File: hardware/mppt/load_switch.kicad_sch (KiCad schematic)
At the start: 13 parts, among them Q901 Q_NMOS_SGD, Q902 Q_NMOS_SGD, U901 TPSI3050

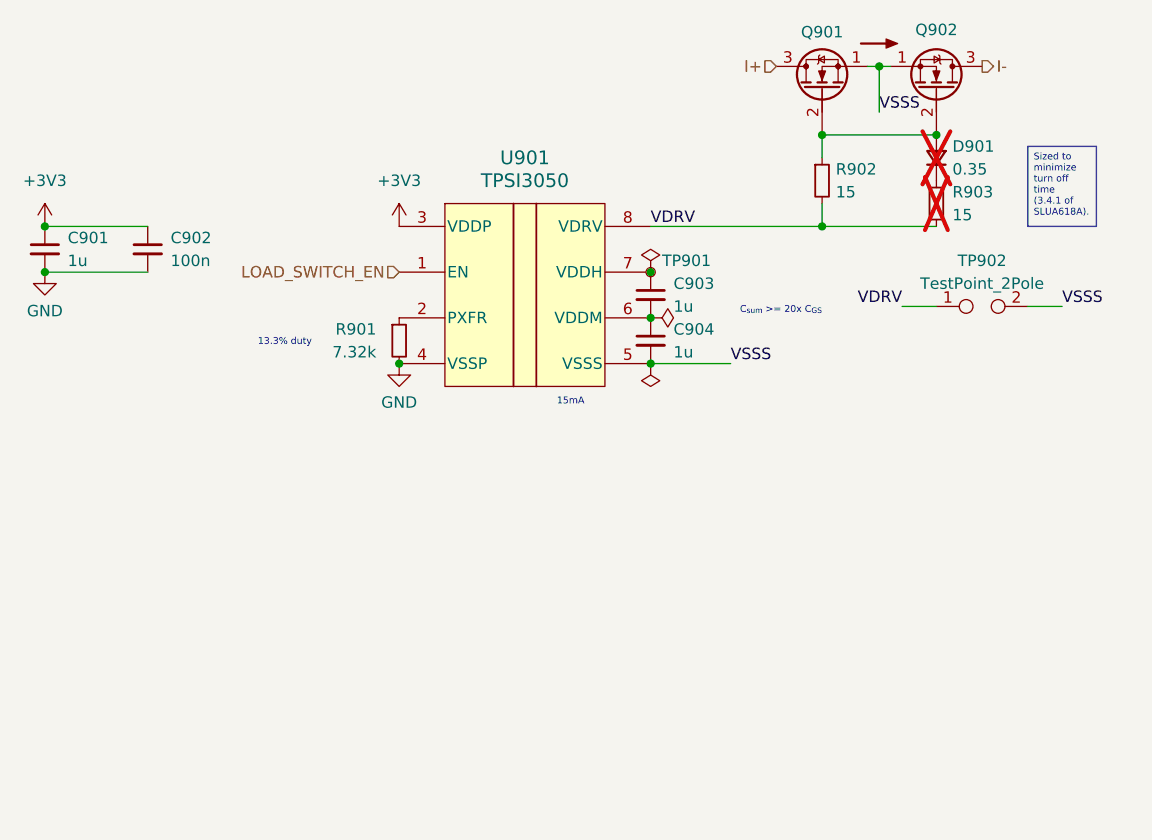
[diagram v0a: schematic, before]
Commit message: run through mppt sch, going through bom
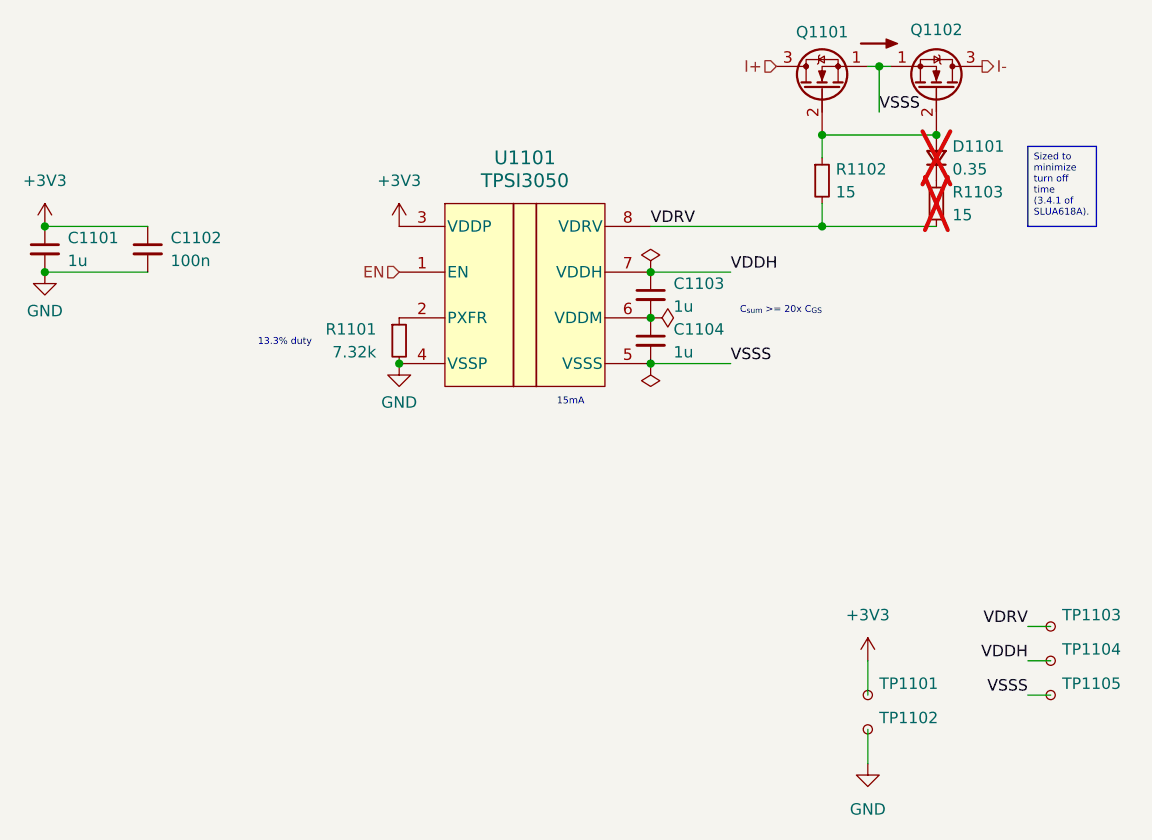
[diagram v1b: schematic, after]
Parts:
- removed TP901: TestPoint_Small, TestPoint:TestPoint_Keystone_5000-5004_Miniature, symbol Connector:TestPoint_Small
- removed TP902: TestPoint_2Pole, symbol Connector:TestPoint_2Pole
- added TP1101, TP1102: TestPoint_Small, TestPoint:TestPoint_Pad_D1.0mm, symbol Connector:TestPoint_Small
- added TP1103, TP1104, TP1105: TestPoint_Small, symbol Connector:TestPoint_Small
- C1101: renamed from C901; footprint Capacitor_SMD:C_0805_2012Metric_Pad1.18x1.45mm_HandSolder -> (none); Manufacturer Samsung Microelectronics -> Samsung Electro-Mechanics; Notes 3.3V -> 3.3V Rating
- C1102: renamed from C902; footprint Capacitor_SMD:C_0805_2012Metric_Pad1.18x1.45mm_HandSolder -> (none); Manufacturer Samsung Microelectronics -> Samsung Electro-Mechanics; Notes 3.3V -> 3.3V Rating
- C1103: renamed from C903; footprint Capacitor_SMD:C_0805_2012Metric_Pad1.18x1.45mm_HandSolder -> (none); Manufacturer Samsung Microelectronics -> Samsung Electro-Mechanics; Notes 10V -> 10V Rating
- C1104: renamed from C904; footprint Capacitor_SMD:C_0805_2012Metric_Pad1.18x1.45mm_HandSolder -> (none); Manufacturer Samsung Microelectronics -> Samsung Electro-Mechanics; Notes 10V -> 10V Rating
- U1101: renamed from U901; Distributor Texas Instruments -> (none)
- renumbered D901 to D1101, Q901 to Q1101, Q902 to Q1102, R901 to R1101, R902 to R1102, R903 to R1103
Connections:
- net +3V3: now also TP1101.1
- net GND: now also TP1102.1
- net VDRV: now also TP1103.1
- net VSSS: now also TP1105.1
- net VDDH: now reaches C1103.1, U1101.7 (VDDH)
- net VDDH: now also TP1104.1
- net LOAD_SWITCH_EN renamed EN

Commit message: update final missing pieces for sch, moving to bom pop
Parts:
- D1101: symbol Device:D_Small -> Device:D_Schottky_Small; Notes (none) -> Low forward voltage drop.
- R1101, R1102, R1103: footprint Resistor_SMD:R_0805_2012Metric_Pad1.20x1.40mm_HandSolder -> (none)
- TP1103, TP1104, TP1105: footprint (none) -> TestPoint:TestPoint_Pad_D1.0mm
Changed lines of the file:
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@@
 			)
 		)
-		(property "Footprint" ""
+		(property "Footprint" "TestPoint:TestPoint_Pad_D1.0mm"
 			(at 193.04 149.86 0)
 			(effects
@@
 			)
 		)
-		(property "Footprint" ""
+		(property "Footprint" "TestPoint:TestPoint_Pad_D1.0mm"
 			(at 193.04 146.05 0)
 			(effects
@@
 			)
 		)
-		(property "Footprint" "Resistor_SMD:R_0805_2012Metric_Pad1.20x1.40mm_HandSolder"
+		(property "Footprint" ""
 			(at 162.56 92.71 0)
 			(effects
@@
 			)
 		)
-		(property "Footprint" "Resistor_SMD:R_0805_2012Metric_Pad1.20x1.40mm_HandSolder"
+		(property "Footprint" ""
 			(at 115.57 110.49 0)
 			(effects
@@
 	)
 	(symbol
-		(lib_id "Device:D_Small")
+		(lib_id "Device:D_Schottky_Small")
 		(at 175.26 90.17 90)
 		(unit 1)
@@
 			)
 		)
-		(property "Datasheet" "https://www.mouser.com/datasheet/2/115/DIOD_S_A0002960396_1-2542090.pdf"
+		(property "Datasheet" "~"
 			(at 175.26 90.17 90)
 			(effects
@@
 			)
 		)
-		(property "Description" "Diode, small symbol"
+		(property "Description" "Schottky diode, small symbol"
 			(at 175.26 90.17 0)
 			(effects
@@
 			)
 		)
-		(property "Notes" ""
+		(property "Notes" "Low forward voltage drop."
 			(at 175.26 90.17 90)
 			(effects
@@
 			)
 		)
-		(property "Footprint" "Resistor_SMD:R_0805_2012Metric_Pad1.20x1.40mm_HandSolder"
+		(property "Footprint" ""
 			(at 175.26 95.25 0)
 			(effects
@@
 			)
 		)
-		(property "Footprint" ""
+		(property "Footprint" "TestPoint:TestPoint_Pad_D1.0mm"
 			(at 193.04 142.24 0)
 			(effects

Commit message: bom consolidated, starting layout
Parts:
- C1101, C1103, C1104: footprint (none) -> Capacitor_SMD:C_0603_1608Metric_Pad1.08x0.95mm_HandSolder; Manufacturer Samsung Electro-Mechanics -> TDK; P/N (none) -> CGA3E1X7R1V105K080AC
- C1102: footprint (none) -> Capacitor_SMD:C_0402_1005Metric_Pad0.74x0.62mm_HandSolder; Manufacturer Samsung Electro-Mechanics -> TDK; P/N (none) -> CGA2B3X7R1H104K050BB
- D1101: value 0.35 -> Schottky; Notes Low forward voltage drop. -> (none)
- R1101: footprint (none) -> Resistor_SMD:R_0603_1608Metric_Pad0.98x0.95mm_HandSolder; P/N (none) -> CRCW06037K32FKEA
- R1102, R1103: footprint (none) -> Resistor_SMD:R_1210_3225Metric_Pad1.30x2.65mm_HandSolder; P/N (none) -> CRCW121015R0FKEA

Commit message: PCB variant for power regulation breakout.
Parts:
- C1101, C1102, C1103, C1104, Q1101, Q1102, R1101, R1102, TP1101, TP1102, TP1103, TP1104, TP1105, U1101: now not fitted; now left out of the parts list
- D1101, R1103: now left out of the parts list
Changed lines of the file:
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@@
 		(unit 1)
 		(exclude_from_sim no)
-		(in_bom yes)
-		(on_board yes)
-		(dnp no)
+		(in_bom no)
+		(on_board no)
+		(dnp yes)
 		(fields_autoplaced yes)
 		(property "Reference" "U1101"
@@
 		(unit 1)
 		(exclude_from_sim no)
-		(in_bom yes)
-		(on_board yes)
-		(dnp no)
+		(in_bom no)
+		(on_board no)
+		(dnp yes)
 		(property "Reference" "Q1102"
 			(at 175.26 75.946 90)
@@
 		(unit 1)
 		(exclude_from_sim no)
-		(in_bom yes)
-		(on_board yes)
-		(dnp no)
+		(in_bom no)
+		(on_board no)
+		(dnp yes)
 		(fields_autoplaced yes)
 		(property "Reference" "TP1105"
@@
 		(unit 1)
 		(exclude_from_sim no)
-		(in_bom yes)
-		(on_board yes)
-		(dnp no)
+		(in_bom no)
+		(on_board no)
+		(dnp yes)
 		(fields_autoplaced yes)
 		(property "Reference" "TP1104"
@@
 		(unit 1)
 		(exclude_from_sim no)
-		(in_bom yes)
-		(on_board yes)
-		(dnp no)
+		(in_bom no)
+		(on_board no)
+		(dnp yes)
 		(fields_autoplaced yes)
 		(property "Reference" "#FLG01103"
@@
 		(unit 1)
 		(exclude_from_sim no)
-		(in_bom yes)
-		(on_board yes)
-		(dnp no)
+		(in_bom no)
+		(on_board no)
+		(dnp yes)
 		(property "Reference" "R1102"
 			(at 164.084 91.44 0)
@@
 		(unit 1)
 		(exclude_from_sim no)
-		(in_bom yes)
-		(on_board yes)
-		(dnp no)
+		(in_bom no)
+		(on_board no)
+		(dnp yes)
 		(property "Reference" "R1101"
 			(at 113.03 109.2199 0)
@@
 		(unit 1)
 		(exclude_from_sim no)
-		(in_bom yes)
-		(on_board yes)
-		(dnp no)
+		(in_bom no)
+		(on_board no)
+		(dnp yes)
 		(fields_autoplaced yes)
 		(property "Reference" "#PWR01101"
@@
 		(unit 1)
 		(exclude_from_sim no)
-		(in_bom yes)
-		(on_board yes)
-		(dnp no)
+		(in_bom no)
+		(on_board no)
+		(dnp yes)
 		(fields_autoplaced yes)
 		(property "Reference" "#FLG01102"
@@
 		(unit 1)
 		(exclude_from_sim no)
-		(in_bom yes)
-		(on_board yes)
-		(dnp no)
+		(in_bom no)
+		(on_board no)
+		(dnp yes)
 		(fields_autoplaced yes)
 		(property "Reference" "#PWR01103"
@@
 		(in_bom no)
 		(on_board no)
-		(dnp no)
+		(dnp yes)
 		(fields_autoplaced yes)
 		(property "Reference" "#SYM1101"
@@
 		(unit 1)
 		(exclude_from_sim no)
-		(in_bom yes)
-		(on_board yes)
+		(in_bom no)
+		(on_board no)
 		(dnp yes)
 		(property "Reference" "D1101"
@@
 		(unit 1)
 		(exclude_from_sim no)
-		(in_bom yes)
-		(on_board yes)
+		(in_bom no)
+		(on_board no)
 		(dnp yes)
 		(property "Reference" "R1103"
@@
 		(unit 1)
 		(exclude_from_sim no)
-		(in_bom yes)
-		(on_board yes)
-		(dnp no)
+		(in_bom no)
+		(on_board no)
+		(dnp yes)
 		(fields_autoplaced yes)
 		(property "Reference" "#PWR01106"
@@
 		(unit 1)
 		(exclude_from_sim no)
-		(in_bom yes)
-		(on_board yes)
-		(dnp no)
+		(in_bom no)
+		(on_board no)
+		(dnp yes)
 		(fields_autoplaced yes)
 		(property "Reference" "C1103"
@@
 		(unit 1)
 		(exclude_from_sim no)
-		(in_bom yes)
-		(on_board yes)
-		(dnp no)
+		(in_bom no)
+		(on_board no)
+		(dnp yes)
 		(fields_autoplaced yes)
 		(property "Reference" "C1101"
@@
 		(unit 1)
 		(exclude_from_sim no)
-		(in_bom yes)
-		(on_board yes)
-		(dnp no)
+		(in_bom no)
+		(on_board no)
+		(dnp yes)
 		(property "Reference" "#PWR01104"
 			(at 115.57 119.38 0)
@@
 		(unit 1)
 		(exclude_from_sim no)
-		(in_bom yes)
-		(on_board yes)
-		(dnp no)
+		(in_bom no)
+		(on_board no)
+		(dnp yes)
 		(fields_autoplaced yes)
 		(property "Reference" "C1102"
@@
 		(unit 1)
 		(exclude_from_sim no)
-		(in_bom yes)
-		(on_board yes)
-		(dnp no)
+		(in_bom no)
+		(on_board no)
+		(dnp yes)
 		(fields_autoplaced yes)
 		(property "Reference" "C1104"
@@
 		(unit 1)
 		(exclude_from_sim no)
-		(in_bom yes)
-		(on_board yes)
-		(dnp no)
+		(in_bom no)
+		(on_board no)
+		(dnp yes)
 		(property "Reference" "#PWR01102"
 			(at 76.2 109.22 0)
@@
 		(unit 1)
 		(exclude_from_sim no)
-		(in_bom yes)
-		(on_board yes)
-		(dnp no)
+		(in_bom no)
+		(on_board no)
+		(dnp yes)
 		(fields_autoplaced yes)
 		(property "Reference" "Q1101"
@@
 		(unit 1)
 		(exclude_from_sim no)
-		(in_bom yes)
-		(on_board yes)
-		(dnp no)
+		(in_bom no)
+		(on_board no)
+		(dnp yes)
 		(fields_autoplaced yes)
 		(property "Reference" "TP1102"
@@
 		(unit 1)
 		(exclude_from_sim no)
-		(in_bom yes)
-		(on_board yes)
-		(dnp no)
+		(in_bom no)
+		(on_board no)
+		(dnp yes)
 		(fields_autoplaced yes)
 		(property "Reference" "TP1103"
@@
 		(unit 1)
 		(exclude_from_sim no)
-		(in_bom yes)
-		(on_board yes)
-		(dnp no)
+		(in_bom no)
+		(on_board no)
+		(dnp yes)
 		(fields_autoplaced yes)
 		(property "Reference" "#FLG01101"
@@
 		(unit 1)
 		(exclude_from_sim no)
-		(in_bom yes)
-		(on_board yes)
-		(dnp no)
+		(in_bom no)
+		(on_board no)
+		(dnp yes)
 		(fields_autoplaced yes)
 		(property "Reference" "TP1101"
@@
 		(unit 1)
 		(exclude_from_sim no)
-		(in_bom yes)
-		(on_board yes)
-		(dnp no)
+		(in_bom no)
+		(on_board no)
+		(dnp yes)
 		(fields_autoplaced yes)
 		(property "Reference" "#PWR01105"

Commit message: converter schematic and layout.
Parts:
- C1101, C1102, C1103, C1104, D1101, Q1101, Q1102, R1101, R1102, R1103, TP1101, TP1102, TP1103, TP1104, TP1105, U1101: now fitted; now in the parts list
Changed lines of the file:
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@@
 		(unit 1)
 		(exclude_from_sim no)
-		(in_bom no)
-		(on_board no)
-		(dnp yes)
+		(in_bom yes)
+		(on_board yes)
+		(dnp no)
 		(fields_autoplaced yes)
 		(property "Reference" "U1101"
@@
 		(unit 1)
 		(exclude_from_sim no)
-		(in_bom no)
-		(on_board no)
-		(dnp yes)
+		(in_bom yes)
+		(on_board yes)
+		(dnp no)
 		(property "Reference" "Q1102"
 			(at 175.26 75.946 90)
@@
 		(unit 1)
 		(exclude_from_sim no)
-		(in_bom no)
-		(on_board no)
-		(dnp yes)
+		(in_bom yes)
+		(on_board yes)
+		(dnp no)
 		(fields_autoplaced yes)
 		(property "Reference" "TP1105"
@@
 		(unit 1)
 		(exclude_from_sim no)
-		(in_bom no)
-		(on_board no)
-		(dnp yes)
+		(in_bom yes)
+		(on_board yes)
+		(dnp no)
 		(fields_autoplaced yes)
 		(property "Reference" "TP1104"
@@
 		(unit 1)
 		(exclude_from_sim no)
-		(in_bom no)
-		(on_board no)
-		(dnp yes)
+		(in_bom yes)
+		(on_board yes)
+		(dnp no)
 		(fields_autoplaced yes)
 		(property "Reference" "#FLG01103"
@@
 		(unit 1)
 		(exclude_from_sim no)
-		(in_bom no)
-		(on_board no)
-		(dnp yes)
+		(in_bom yes)
+		(on_board yes)
+		(dnp no)
 		(property "Reference" "R1102"
 			(at 164.084 91.44 0)
@@
 		(unit 1)
 		(exclude_from_sim no)
-		(in_bom no)
-		(on_board no)
-		(dnp yes)
+		(in_bom yes)
+		(on_board yes)
+		(dnp no)
 		(property "Reference" "R1101"
 			(at 113.03 109.2199 0)
@@
 		(unit 1)
 		(exclude_from_sim no)
-		(in_bom no)
-		(on_board no)
-		(dnp yes)
+		(in_bom yes)
+		(on_board yes)
+		(dnp no)
 		(fields_autoplaced yes)
 		(property "Reference" "#PWR01101"
@@
 		(unit 1)
 		(exclude_from_sim no)
-		(in_bom no)
-		(on_board no)
-		(dnp yes)
+		(in_bom yes)
+		(on_board yes)
+		(dnp no)
 		(fields_autoplaced yes)
 		(property "Reference" "#FLG01102"
@@
 		(unit 1)
 		(exclude_from_sim no)
-		(in_bom no)
-		(on_board no)
-		(dnp yes)
+		(in_bom yes)
+		(on_board yes)
+		(dnp no)
 		(fields_autoplaced yes)
 		(property "Reference" "#PWR01103"
@@
 		(unit 1)
 		(exclude_from_sim no)
-		(in_bom no)
-		(on_board no)
-		(dnp yes)
+		(in_bom yes)
+		(on_board yes)
+		(dnp no)
 		(fields_autoplaced yes)
 		(property "Reference" "#SYM1101"
@@
 		(unit 1)
 		(exclude_from_sim no)
-		(in_bom no)
-		(on_board no)
-		(dnp yes)
+		(in_bom yes)
+		(on_board yes)
+		(dnp no)
 		(property "Reference" "D1101"
 			(at 177.038 88.9 90)
@@
 		(unit 1)
 		(exclude_from_sim no)
-		(in_bom no)
-		(on_board no)
-		(dnp yes)
+		(in_bom yes)
+		(on_board yes)
+		(dnp no)
 		(property "Reference" "R1103"
 			(at 177.038 93.98 0)
@@
 		(unit 1)
 		(exclude_from_sim no)
-		(in_bom no)
-		(on_board no)
-		(dnp yes)
+		(in_bom yes)
+		(on_board yes)
+		(dnp no)
 		(fields_autoplaced yes)
 		(property "Reference" "#PWR01106"
@@
 		(unit 1)
 		(exclude_from_sim no)
-		(in_bom no)
-		(on_board no)
-		(dnp yes)
+		(in_bom yes)
+		(on_board yes)
+		(dnp no)
 		(fields_autoplaced yes)
 		(property "Reference" "C1103"
@@
 		(unit 1)
 		(exclude_from_sim no)
-		(in_bom no)
-		(on_board no)
-		(dnp yes)
+		(in_bom yes)
+		(on_board yes)
+		(dnp no)
 		(fields_autoplaced yes)
 		(property "Reference" "C1101"
@@
 		(unit 1)
 		(exclude_from_sim no)
-		(in_bom no)
-		(on_board no)
-		(dnp yes)
+		(in_bom yes)
+		(on_board yes)
+		(dnp no)
 		(property "Reference" "#PWR01104"
 			(at 115.57 119.38 0)
@@
 		(unit 1)
 		(exclude_from_sim no)
-		(in_bom no)
-		(on_board no)
-		(dnp yes)
+		(in_bom yes)
+		(on_board yes)
+		(dnp no)
 		(fields_autoplaced yes)
 		(property "Reference" "C1102"
@@
 		(unit 1)
 		(exclude_from_sim no)
-		(in_bom no)
-		(on_board no)
-		(dnp yes)
+		(in_bom yes)
+		(on_board yes)
+		(dnp no)
 		(fields_autoplaced yes)
 		(property "Reference" "C1104"
@@
 		(unit 1)
 		(exclude_from_sim no)
-		(in_bom no)
-		(on_board no)
-		(dnp yes)
+		(in_bom yes)
+		(on_board yes)
+		(dnp no)
 		(property "Reference" "#PWR01102"
 			(at 76.2 109.22 0)
@@
 		(unit 1)
 		(exclude_from_sim no)
-		(in_bom no)
-		(on_board no)
-		(dnp yes)
+		(in_bom yes)
+		(on_board yes)
+		(dnp no)
 		(fields_autoplaced yes)
 		(property "Reference" "Q1101"
@@
 		(unit 1)
 		(exclude_from_sim no)
-		(in_bom no)
-		(on_board no)
-		(dnp yes)
+		(in_bom yes)
+		(on_board yes)
+		(dnp no)
 		(fields_autoplaced yes)
 		(property "Reference" "TP1102"
@@
 		(unit 1)
 		(exclude_from_sim no)
-		(in_bom no)
-		(on_board no)
-		(dnp yes)
+		(in_bom yes)
+		(on_board yes)
+		(dnp no)
 		(fields_autoplaced yes)
 		(property "Reference" "TP1103"
@@
 		(unit 1)
 		(exclude_from_sim no)
-		(in_bom no)
-		(on_board no)
-		(dnp yes)
+		(in_bom yes)
+		(on_board yes)
+		(dnp no)
 		(fields_autoplaced yes)
 		(property "Reference" "#FLG01101"
@@
 		(unit 1)
 		(exclude_from_sim no)
-		(in_bom no)
-		(on_board no)
-		(dnp yes)
+		(in_bom yes)
+		(on_board yes)
+		(dnp no)
 		(fields_autoplaced yes)
 		(property "Reference" "TP1101"
@@
 		(unit 1)
 		(exclude_from_sim no)
-		(in_bom no)
-		(on_board no)
-		(dnp yes)
+		(in_bom yes)
+		(on_board yes)
+		(dnp no)
 		(fields_autoplaced yes)
 		(property "Reference" "#PWR01105"

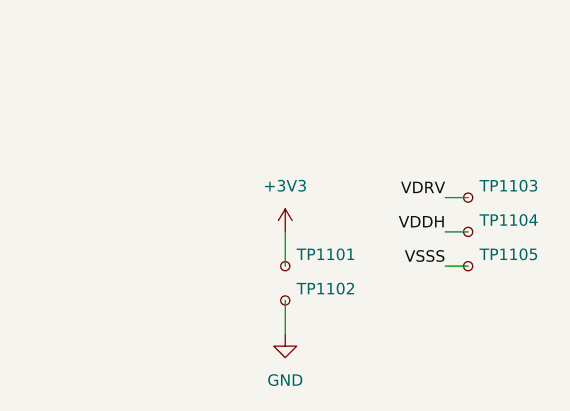
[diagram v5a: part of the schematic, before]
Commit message: remove testpoints, integrat 60% of layout
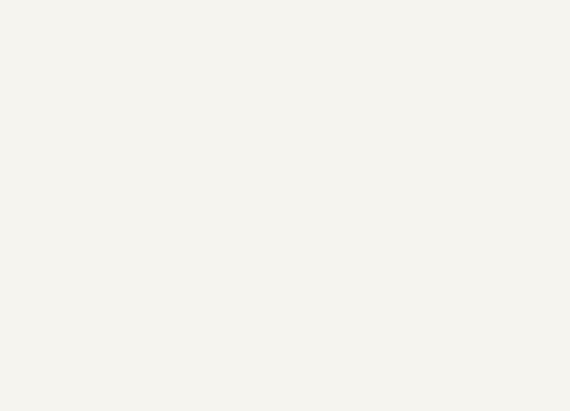
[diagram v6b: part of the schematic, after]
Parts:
- removed TP1101, TP1102, TP1103, TP1104, TP1105: TestPoint_Small, TestPoint:TestPoint_Pad_D1.0mm, symbol Connector:TestPoint_Small
- R1102, R1103: footprint Resistor_SMD:R_1210_3225Metric_Pad1.30x2.65mm_HandSolder -> Resistor_SMD:R_0603_1608Metric; P/N CRCW121015R0FKEA -> CRCW060315R0FKEAHP
